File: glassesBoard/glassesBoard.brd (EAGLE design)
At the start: 82.9 x 29.2 mm, 122 parts, among them J1 BM10NB(0.8)-16DS-0.4V(51), J2 DF30FC-30DS-0.4V, J3 S2B-XH-A(LF)(SN), J4 GRPB042MWCN-RC, J5 0787324001, J7 105450-0101, U10 ATTINY20-MMH, U11 SN65LVDS822VQFN48, U12 NLAS2750, U13 NX3020NAK, U14 SSM3J338RSOT-23F, U15 NX3020NAK, U16 SSM3J338RSOT-23F, U17 NX3020NAK, U18 2.8, U19 TCR2EF15SOT-25, U2 TPS613222A, U20 MICROSD, U21 MCP73833, U22 FXMA2104UMX, U23 NX3020NAK, U24 FXMA2104UMX, U25 FXMA2104UMX, U3 1.8, U4 3.3, U5 SSM3J338RSOT-23F, U6 SSM3J338RSOT-23F, U7 SN65DSI83-Q1S-PQFP-G64, U8 IQS263BDFN10, U9 NX3020NAK

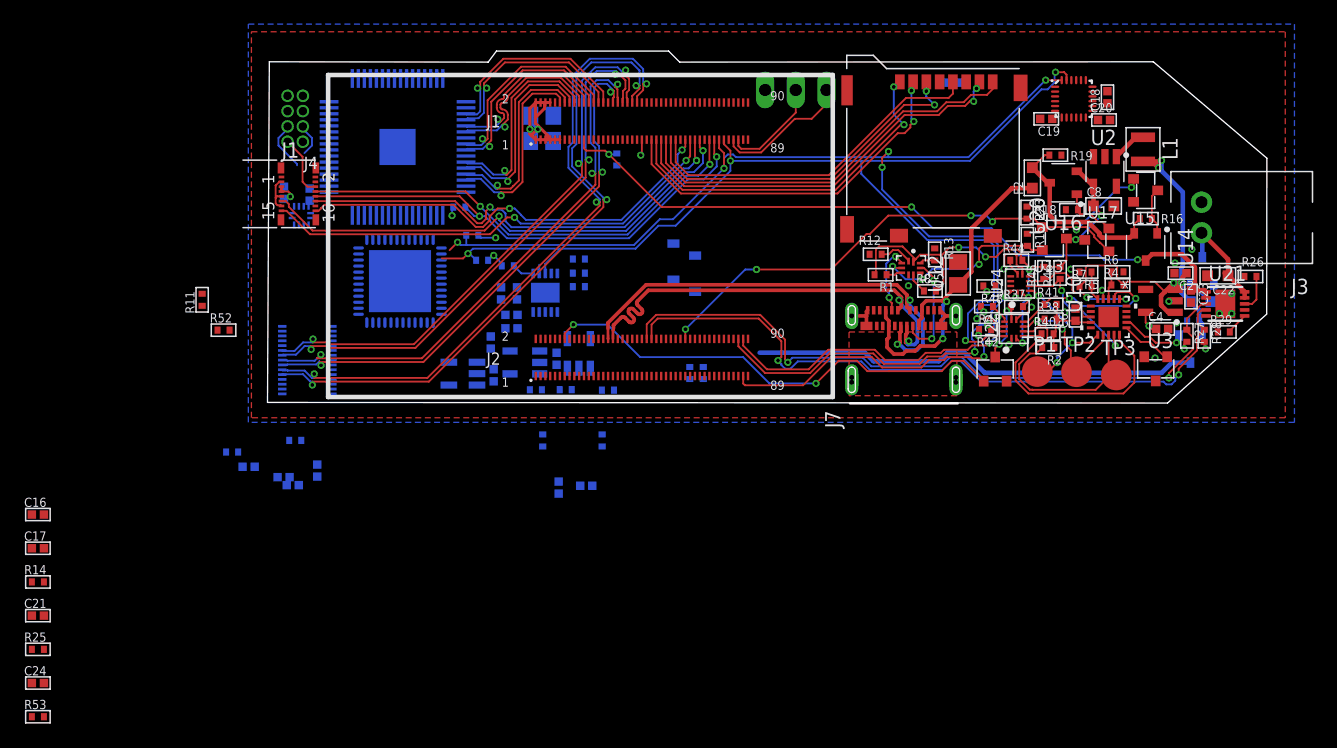
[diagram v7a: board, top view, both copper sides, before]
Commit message: Added display connector, dip switch, 10V supply
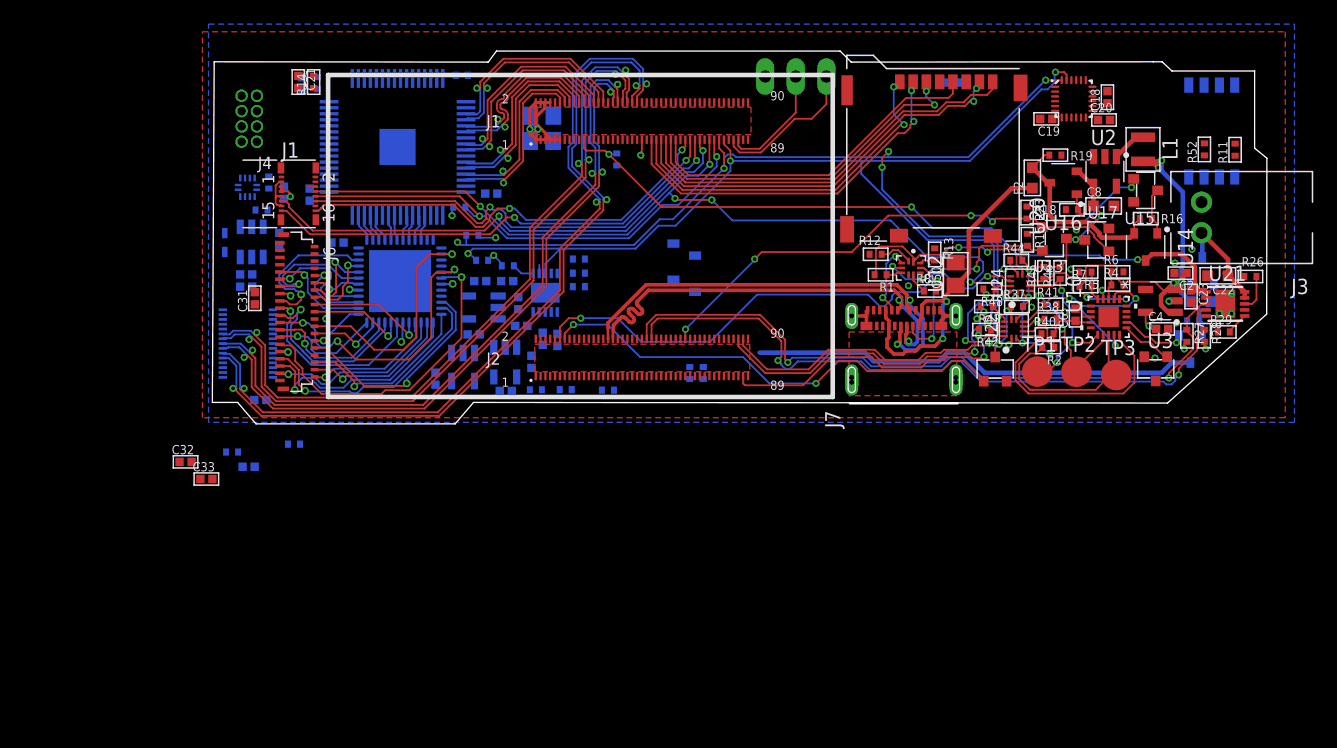
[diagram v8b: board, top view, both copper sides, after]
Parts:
- added C32, C33: 100nF, thanics-capacitor:C0402
- added C34, C35, C36: 1uF, thanics-capacitor:C0402
- added D1: SDM03U40-7SC79, glasses:SOD1608X70
- added J6: FH26W-39S-0.3SHW, thanics-connector:FH26W-39S-0.3SHW
- added S1: 218-4LPST, glasses:218-4LPST
- added U26: LM2665M6XSOT23-6, glasses:SOT95P280X145-6
- moved R11 86.5 mm to (84.5, 21.0)
- moved R52 82.7 mm to (81.9, 21.0), turned to 90 degrees
- moved R53 63.8 mm to (20.4, 27.1), flipped to the bottom, turned to 180 degrees
- moved R25 52.3 mm to (8.38, 26.5), flipped to the bottom, turned to 270 degrees
- moved C21 49.2 mm to (6.81, 26.6), turned to 270 degrees
- moved C17 47.7 mm to (22.8, 17.3), flipped to the bottom, turned to 180 degrees
- moved R14 47.3 mm to (8.08, 26.6), turned to 90 degrees
- moved C24 44.2 mm to (10.1, 13.3), flipped to the bottom
- moved C16 42.0 mm to (7.16, 26.5), flipped to the bottom, turned to 90 degrees
- moved R49 34.1 mm to (3.76, 16.0), turned to 180 degrees
- moved R47 31.2 mm to (4.37, 18.2)
- moved C5 19.1 mm to (21.9, 10.1)
- moved C3 17.6 mm to (24.1, 10.1), turned to 180 degrees
- moved C31 15.8 mm to (3.20, 8.64), flipped to the top, turned to 90 degrees
- moved C13 12.4 mm to (18.2, 1.97)
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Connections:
- removed net !TOUCH_INT: R39.1, U8.6
- new net +10V: C35.1, D1.C, J6.4, U26.5
- new net B0: J6.38, U11.4
- new net B1: J6.37, U11.3
- new net B2: J6.36, U11.2
- new net B3: J6.35, U11.1
- new net B4: J6.34, U11.48
- new net B5: J6.33, U11.47
- new net B6: J6.30, U11.46
- new net B7: J6.29, U11.42
- new net CABC: J6.32
- new net CLKX: J6.23, U11.41
- new net COM: C32.1, J6.2
- new net CSTN: C33.1, J6.3
- new net DE: J6.24, U11.38
- new net G0: J6.28, U11.13
- new net G1: J6.27, U11.12
- new net G2: J6.26, U11.11
- new net G3: J6.25, U11.10
- new net G4: J6.21, U11.9
- new net G5: J6.20, U11.8
- new net G6: J6.19, U11.7
- new net G7: J6.18, U11.5
- new net N$38: C34.1, U26.6
- new net N$40: C34.2, U26.3
- new net N$42: C35.2, C36.1
- new net R0: J6.17, U11.22
- new net R1: J6.16, U11.21
- new net R2: J6.14, U11.20
- new net R3: J6.13, U11.19
- new net R4: J6.12, U11.18
- new net R5: J6.11, U11.16
- new net R6: J6.10, U11.15
- new net R7: J6.9, U11.14
- new net RESETB: J6.6
- new net SCL: J6.8
- new net SDA: J6.7
- new net TEST_HV: J6.1
- net !TOUCH_INT_1V8: now also R39.1, U8.6
- net +1V8: now also J6.15, J6.31, S1.3
- net +5V: now also D1.A, U26.1
- net BOOT_CONFIG_1: now also S1.6
- net FORCED_USB_BOOT: now also S1.2
- net GND: now also C32.2, C33.2, C36.2, J6.22, J6.5, S1.7, U26.2, U26.4
- net N$14: now also S1.1
- net N$34: now also S1.5
- net PM_RESIN_N: now also S1.8
- net USB_HS_ID: now also S1.4
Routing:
- net !TOUCH_INT_1V8: track 0.00 -> 45.9 mm, vias 0 -> 2
- net !FINGER_INT_1V8: track 38.7 -> 73.1 mm, vias 2 -> 5
- net B7: track 0.00 -> 26.3 mm, vias 0 -> 1
- net CLKX: track 0.00 -> 23.9 mm, vias 0 -> 3
- net B5: track 0.00 -> 20.7 mm, vias 0 -> 1
- net DE: track 0.00 -> 19.8 mm, vias 0 -> 1
- net B3: track 0.00 -> 18.4 mm, vias 0 -> 1
- net B6: track 0.00 -> 18.2 mm, vias 0 -> 1
- net G6: track 0.00 -> 15.6 mm, vias 0 -> 1
- net G4: track 0.00 -> 15.2 mm, vias 0 -> 1
- net B4: track 0.00 -> 15.0 mm, vias 0 -> 1
- net B1: track 0.00 -> 15.0 mm, vias 0 -> 1
- net MIPI_CSI1_DATA1_P: track 47.5 -> 60.8 mm
- net MIPI_CSI1_DATA1_N: track 46.8 -> 60.1 mm
- net R0: track 0.00 -> 12.8 mm, vias 0 -> 1
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- added copper zone on layer 1, net GND1
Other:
- board size 82.9 x 29.2 mm -> 87.4 x 30.9 mm
